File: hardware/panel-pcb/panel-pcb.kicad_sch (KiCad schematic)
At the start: 131 parts, among them J1 USB_C_Receptacle_USB2.0_16P, J10 RS-485 OUT, J11 12V_OUT, J2 SWD, J3 FSR North, J4 FSR East, J5 12V_IN, J6 FSR South, J7 FSR West, J8 RS-485 IN, J9 INT OUT, SW1 PANEL_ID, SW2 BOOTSEL, SW3 RS-485 Termination, U1 RP2040, U2 THVD1419, U3 W25Q32JV, U4 SN74AHCT125, U5 AMS1117-5.0, U6 AP7361C-33ER-13, U7 USBLC6-2SC6, X1 12MHz

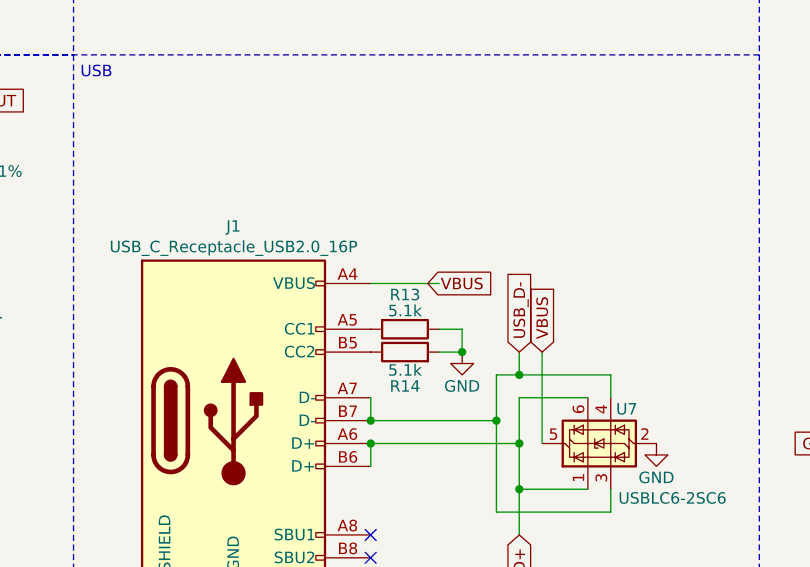
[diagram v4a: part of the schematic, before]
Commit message: Panel PCB: silkscreen positioning pass, verified ERC/DRC exclusions, page settings
- Reposition reference/value silkscreen across the board.
- Fix J1 B1/B12 starved thermal spokes.
- Save C51's edited electrolytic footprint into panel-pcb.pretty as
  CP_Elec_10x10.5_RVT1E471M and re-associate.
- Exclude verified-benign warnings: 25 lib_footprint_mismatch DRC
  false positives (rotation-correlated, content identical to library)
  and lib_symbol_mismatch ERC noise (cached flattened copies of
  derived library symbols, pins verified identical).
- Page settings: A3 -> A4 landscape, title block date/rev refreshed,
  stale mounting-hole placeholder comment removed.

Still pending before fab: silkscreen additions (name/rev/logos/JLC
order-number placeholder), final gerber export.
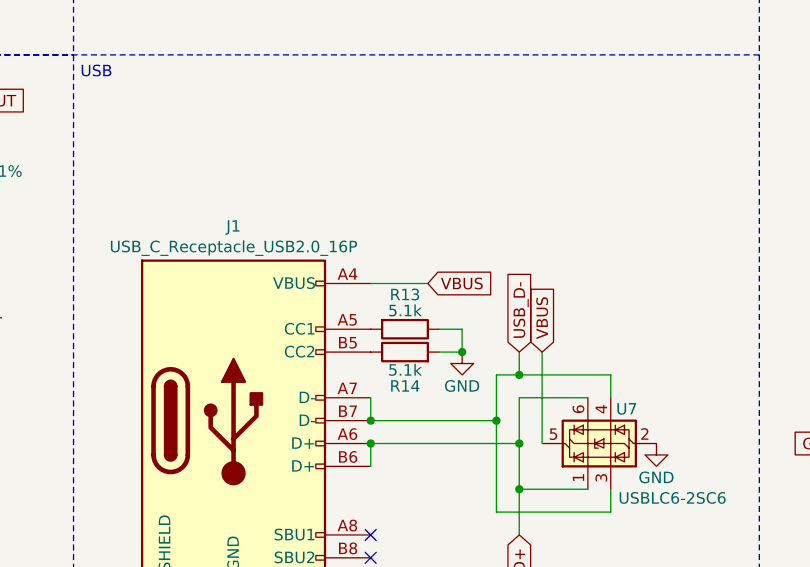
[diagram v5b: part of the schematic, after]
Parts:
- C51: footprint Capacitor_SMD:CP_Elec_10x10.5 -> panel-pcb:CP_Elec_10x10.5_RVT1E471M
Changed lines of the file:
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@@
 		)
 	)
+	(wire
+		(pts
+			(xy 153.67 144.78) (xy 160.02 144.78)
+		)
+		(stroke
+			(width 0)
+			(type default)
+		)
+	)
 	(polyline
 		(pts
@@
 	(wire
 		(pts
-			(xy 153.67 144.78) (xy 161.29 144.78)
-		)
-		(stroke
-			(width 0)
-			(type default)
-		)
-	)
-	(wire
-		(pts
 			(xy 67.31 162.56) (xy 67.31 160.02)
 		)
@@
 			)
 		)
-		(property "Footprint" "Capacitor_SMD:CP_Elec_10x10.5"
+		(property "Footprint" "panel-pcb:CP_Elec_10x10.5_RVT1E471M"
 			(at 294.64 222.25 0)
 			(hide yes)

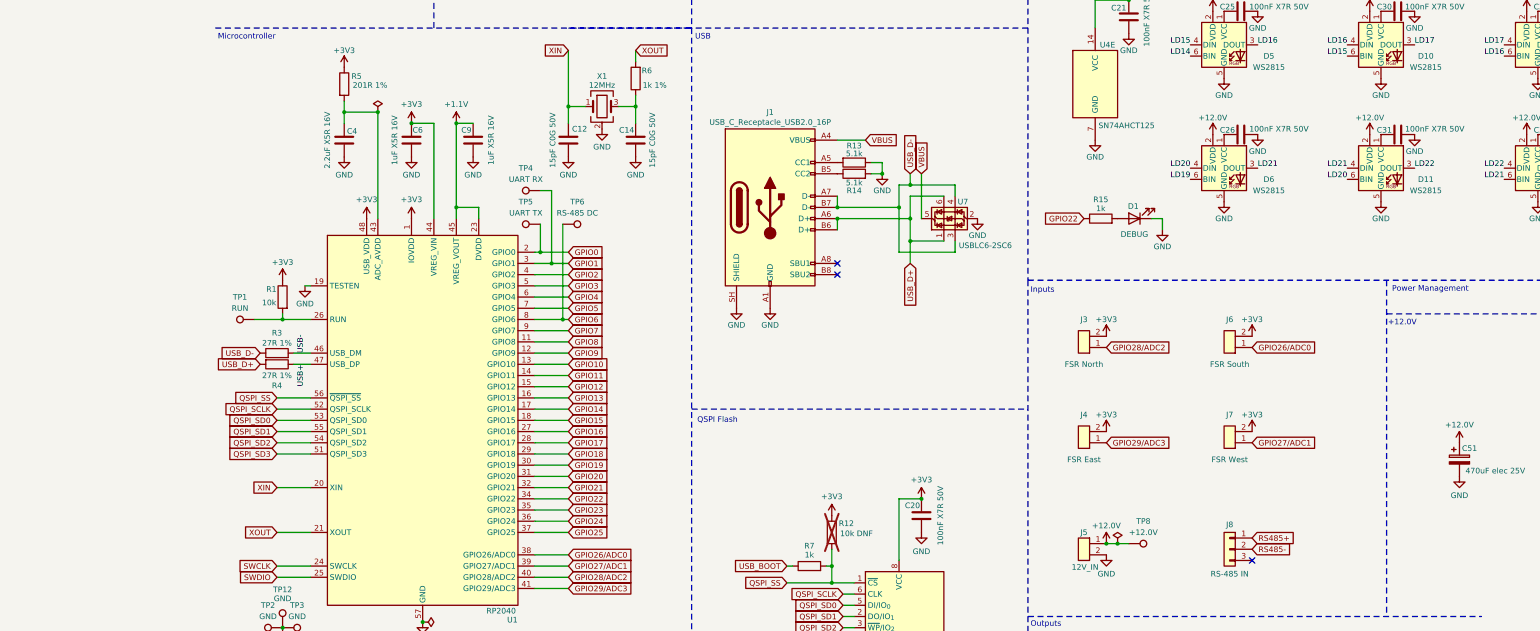
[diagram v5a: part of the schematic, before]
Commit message: Panel PCB: design-review batch 1 - fit R12, lock X1 MPN, metadata fixes
From the AI design review (tmp/review-bundle/ai-review, not tracked):
- R12 QSPI /CS pull-up: DNF -> fitted 10k. The Pi guide's DNF default
  was validated on W25Q128JVS, not W25Q32JV, and RP2040's internal
  QSPI_SS pull-up is not guaranteed during early power-ramp.
- X1 value now names ABM8-272-T3 explicitly (CL=10pF is what the
  15pF/15pF/1k network is calculated for); rationale in Description.
- Fix refdes drift in four Description fields: C10 (U5->U2),
  R2 (SW2->SW3), D12 (J2->J1), D23 (U3->U5).
- Rename In2 zone 9 from '+12.0V' to '+5.0V' to match its net.
- Docs: correct the BOM.md/schematic-plan claim that the WS2815 app
  circuit ties first BIN to the data source - the vendor circuit
  grounds it (schematic/layout change to follow).

ERC 0 errors; DRC 0 violations, 0 unconnected.
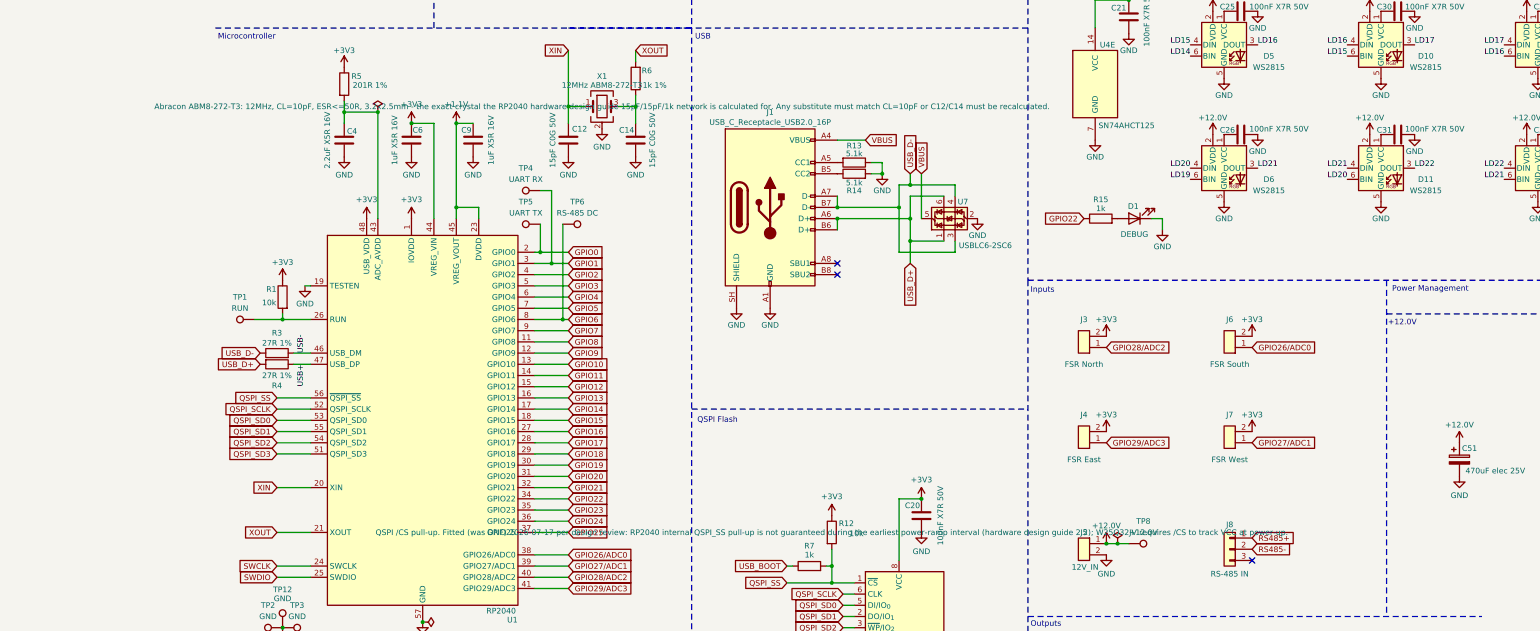
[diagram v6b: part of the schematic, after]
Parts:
- R12: value 10k DNF -> 10k; now fitted
- X1: value 12MHz -> 12MHz ABM8-272-T3
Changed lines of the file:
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@@
 		(on_board yes)
 		(in_pos_files yes)
-		(dnp yes)
+		(dnp no)
 		(property "Reference" "R12"
 			(at 155.702 231.648 0)
@@
 			)
 		)
-		(property "Value" "10k DNF"
+		(property "Value" "10k"
 			(at 157.988 233.934 0)
 			(show_name no)
@@
 			)
 		)
-		(property "Description" ""
+		(property "Description" "QSPI /CS pull-up. Fitted (was DNF) 2026-07-17 per design review: RP2040 internal QSPI_SS pull-up is not guaranteed during the earliest power-ramp interval (hardware design guide 2.2); W25Q32JV requires /CS to track VCC at power-up."
 			(at 152.4 233.68 0)
 			(show_name no)
@@
 			)
 		)
-		(property "Description" "U5 (RS-485 transceiver) VCC decoupling."
+		(property "Description" "U2 (RS-485 transceiver) VCC decoupling."
 			(at 86.36 38.1 0)
 			(hide yes)
@@
 			)
 		)
-		(property "Value" "12MHz"
+		(property "Value" "12MHz ABM8-272-T3"
 			(at 100.33 132.334 0)
 			(show_name no)
@@
 			)
 		)
-		(property "Description" ""
+		(property "Description" "Abracon ABM8-272-T3: 12MHz, CL=10pF, ESR<=50R, 3.2x2.5mm - the exact crystal the RP2040 hardware design guide 15pF/15pF/1k network is calculated for. Any substitute must match CL=10pF or C12/C14 must be recalculated."
 			(at 100.33 137.16 0)
 			(show_name no)
@@
 			)
 		)
-		(property "Description" "Power-OR diode: AMS1117-5.0 output (12V-derived 5V) into V5_OR node. Pin 2 (A/anode) faces U3's VO; pin 1 (K/cathode) faces the V5_OR node. Ultra-low-VF Schottky swap for 1N5819W (2026-07-16): 255mV typ @100mA. Order PMEG3015EH,115 - LCSC C552867."
+		(property "Description" "Power-OR diode: AMS1117-5.0 output (12V-derived 5V) into V5_OR node. Pin 2 (A/anode) faces U5's VO; pin 1 (K/cathode) faces the V5_OR node. Ultra-low-VF Schottky swap for 1N5819W (2026-07-16): 255mV typ @100mA. Order PMEG3015EH,115 - LCSC C552867."
 			(at 353.06 219.71 0)
 			(hide yes)
@@
 			)
 		)
-		(property "Description" "Power-OR diode: USB VBUS into V5_OR node, allows USB-only bench powering/flashing. Pin 2 (A/anode) faces J2's VBUS; pin 1 (K/cathode) faces the V5_OR node. Ultra-low-VF Schottky swap for 1N5819W (2026-07-16): 255mV typ @100mA. Order PMEG3015EH,115 - LCSC C552867."
+		(property "Description" "Power-OR diode: USB VBUS into V5_OR node, allows USB-only bench powering/flashing. Pin 2 (A/anode) faces J1's VBUS; pin 1 (K/cathode) faces the V5_OR node. Ultra-low-VF Schottky swap for 1N5819W (2026-07-16): 255mV typ @100mA. Order PMEG3015EH,115 - LCSC C552867."
 			(at 341.63 190.5 0)
 			(hide yes)
@@
 			)
 		)
-		(property "Description" "RS-485 bus termination resistor. In-circuit only when SW2 pole 1 is in the terminated position."
+		(property "Description" "RS-485 bus termination resistor. In-circuit only when SW3 pole 1 is in the terminated position."
 			(at 44.45 87.63 0)
 			(hide yes)

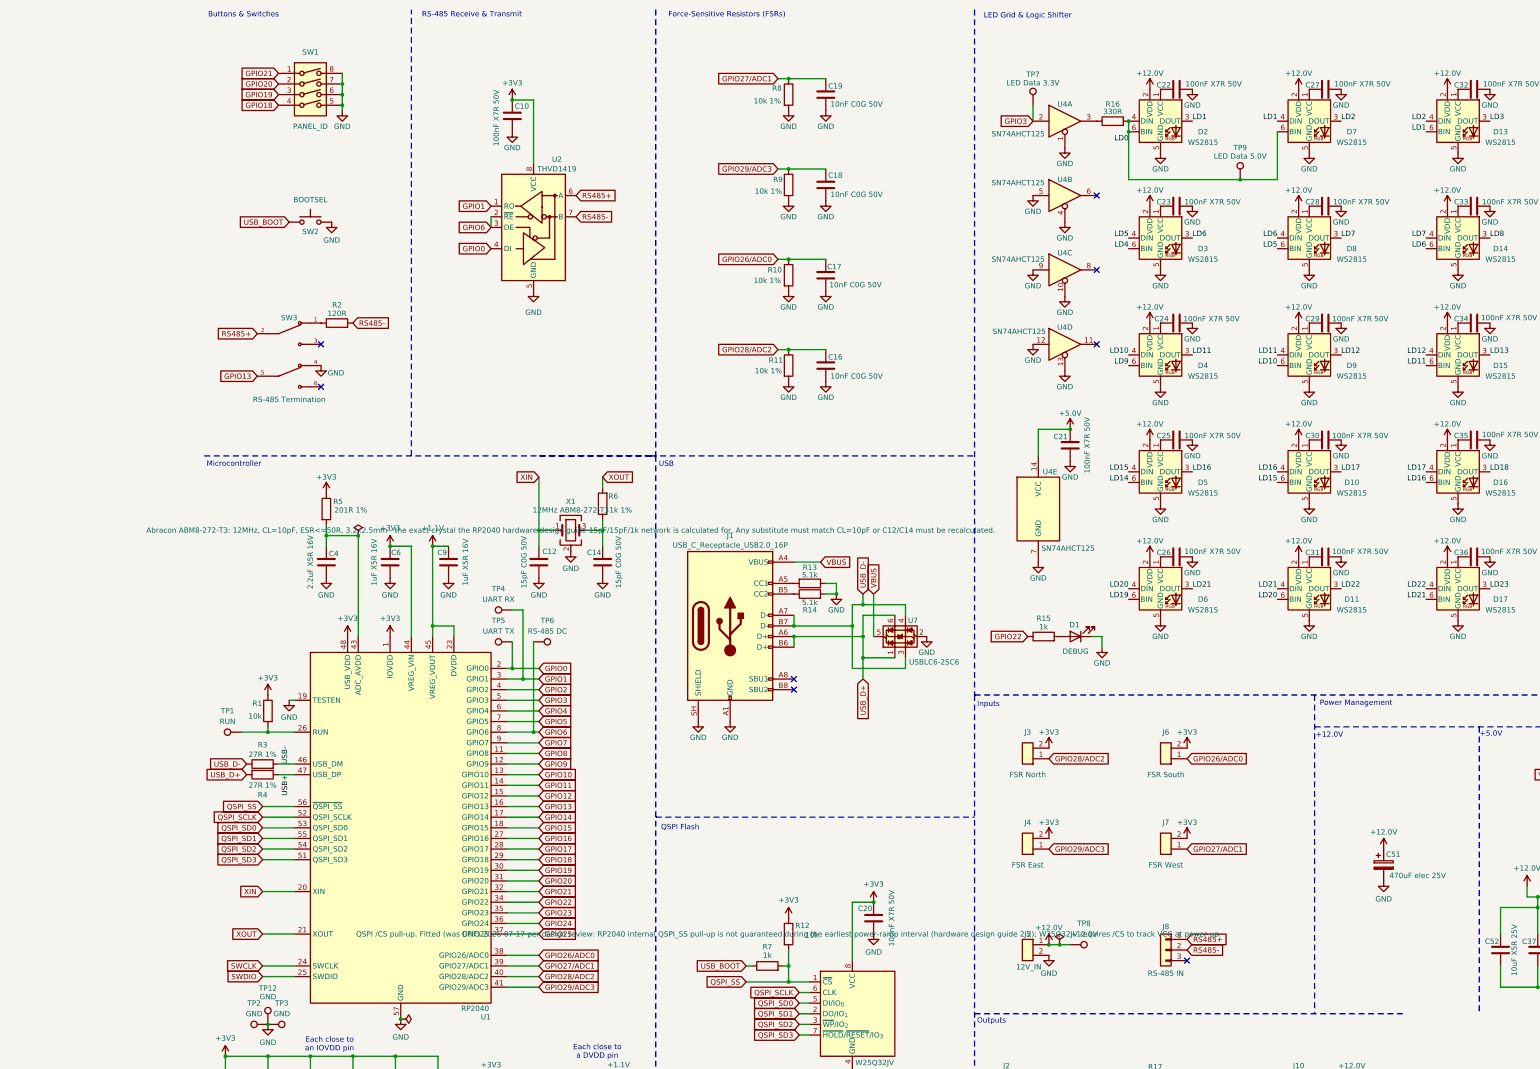
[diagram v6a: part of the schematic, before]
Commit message: Panel PCB: design-review batch 2 - first-BIN ground, 12V sense divider, QSPI margin
- D2.6 (first WS2815 BIN) rewired from /LD0 to GND, matching the
  vendor application circuit (review finding P3-2; the old BOM.md
  claim that the datasheet ties it to the data source was wrong).
- New 12V presence sense: R18 100k from +12.0V, R19 22k to GND,
  C53 100nF filter, midpoint to GPIO17 (U1.28). ~2.16V at 12V,
  ~100uA injection ceiling into an unpowered GPIO. Lets firmware
  gate LED data output on 12V-good so USB-only bench power never
  drives unpowered WS2815 inputs (review finding P4-2).
- QSPI_SD0/SD2 pinch widened 0.09mm -> 0.127mm (was at JLC's
  absolute multilayer minimum spacing; review finding P5-06).
- Board recentered on the new A4 sheet; zones refilled.

ERC 0 errors; DRC 0 violations, 0 unconnected.
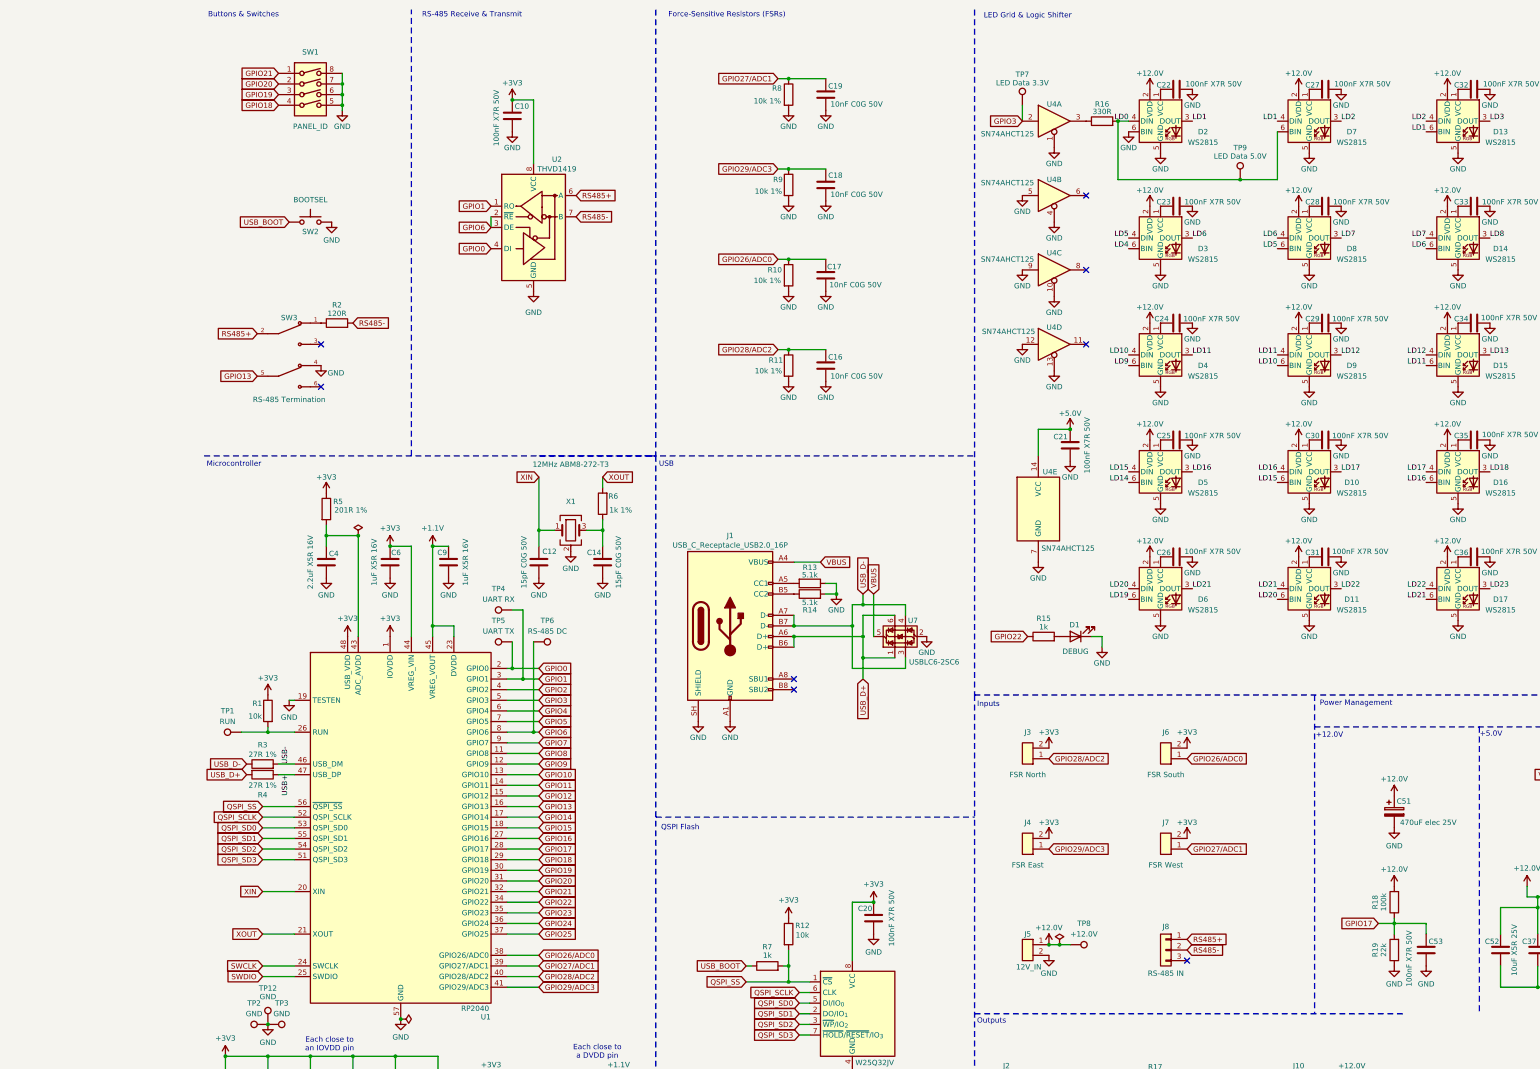
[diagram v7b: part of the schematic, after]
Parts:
- added C53: 100nF X7R 50V, Capacitor_SMD:C_0603_1608Metric, symbol Device:C
- added R18: 100k, Resistor_SMD:R_0603_1608Metric, symbol Device:R
- added R19: 22k, Resistor_SMD:R_0603_1608Metric, symbol Device:R
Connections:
- net +12.0V: now also R18.2
- net GND: now also D2.6 (BIN), C53.1, R19.1
- net GPIO17: now also C53.2, R18.1, R19.2
- net LD0: no longer D2.6 (BIN)
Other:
- moved on the sheet: C51, R16, TP7, U4A, U4B, U4C, U4D
